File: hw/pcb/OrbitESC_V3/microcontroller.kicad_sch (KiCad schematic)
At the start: 63 parts, among them J1 USB_C_Receptacle_USB2.0, J11 CANH, J11 CANL, J11 GND, J11 RX, J11 TX, J8 Micro_SD_Card_Det2, SW1 Reset, SW2 DFU, U1 TLE9250X, U2 AT25SF128A-SHB-T, U3 STM32F446RETx, X1 ASE-24MHz

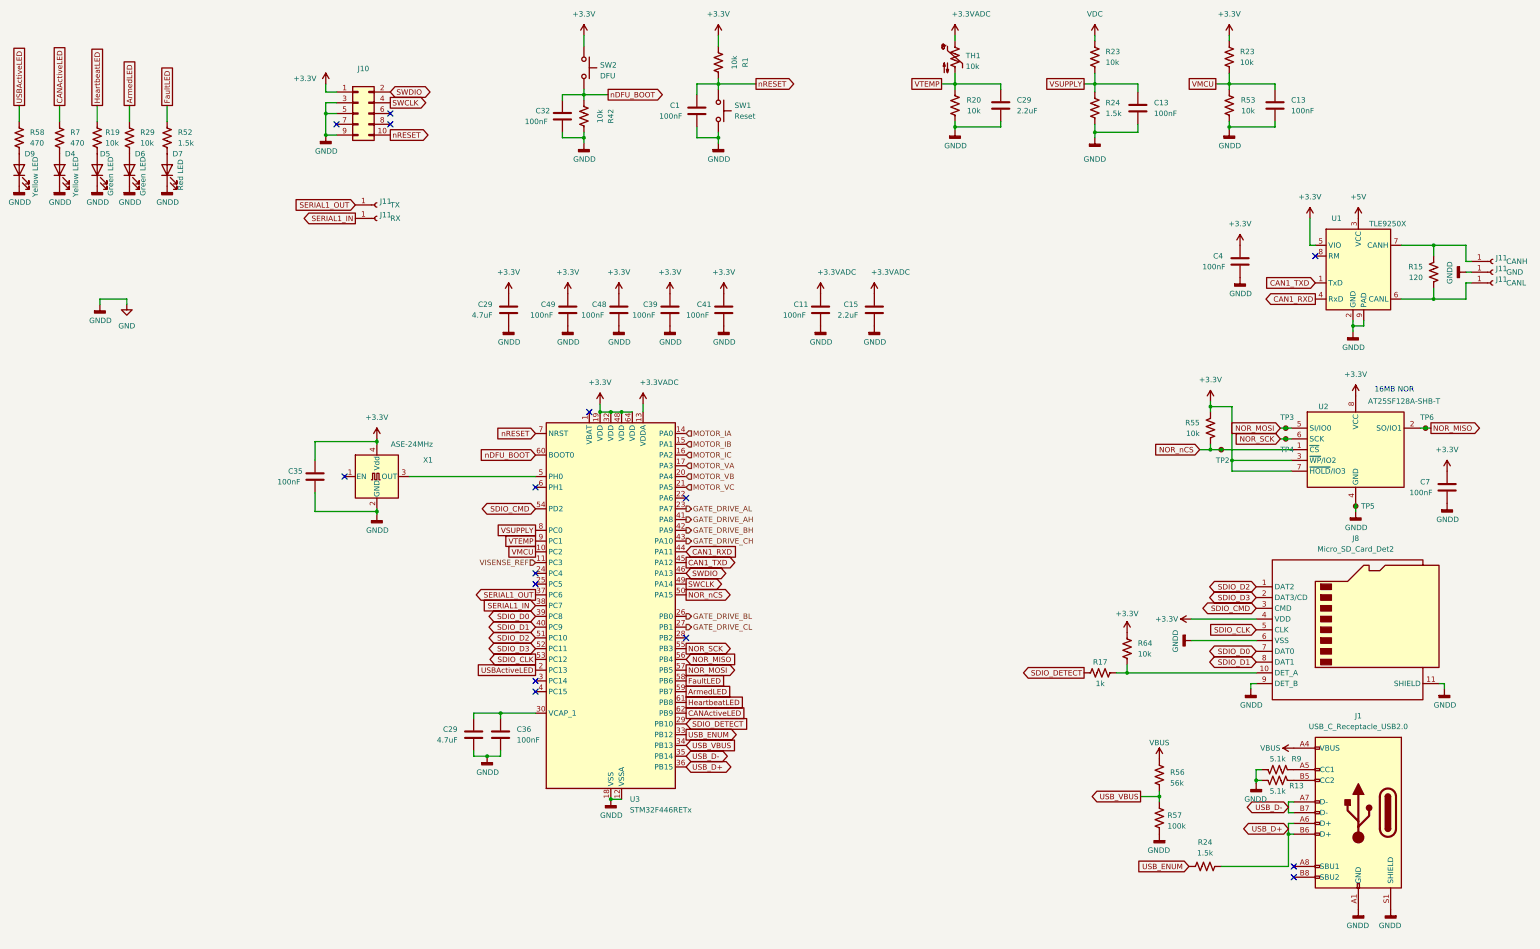
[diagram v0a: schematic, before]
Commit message: Finish initial draft of V3 pcb
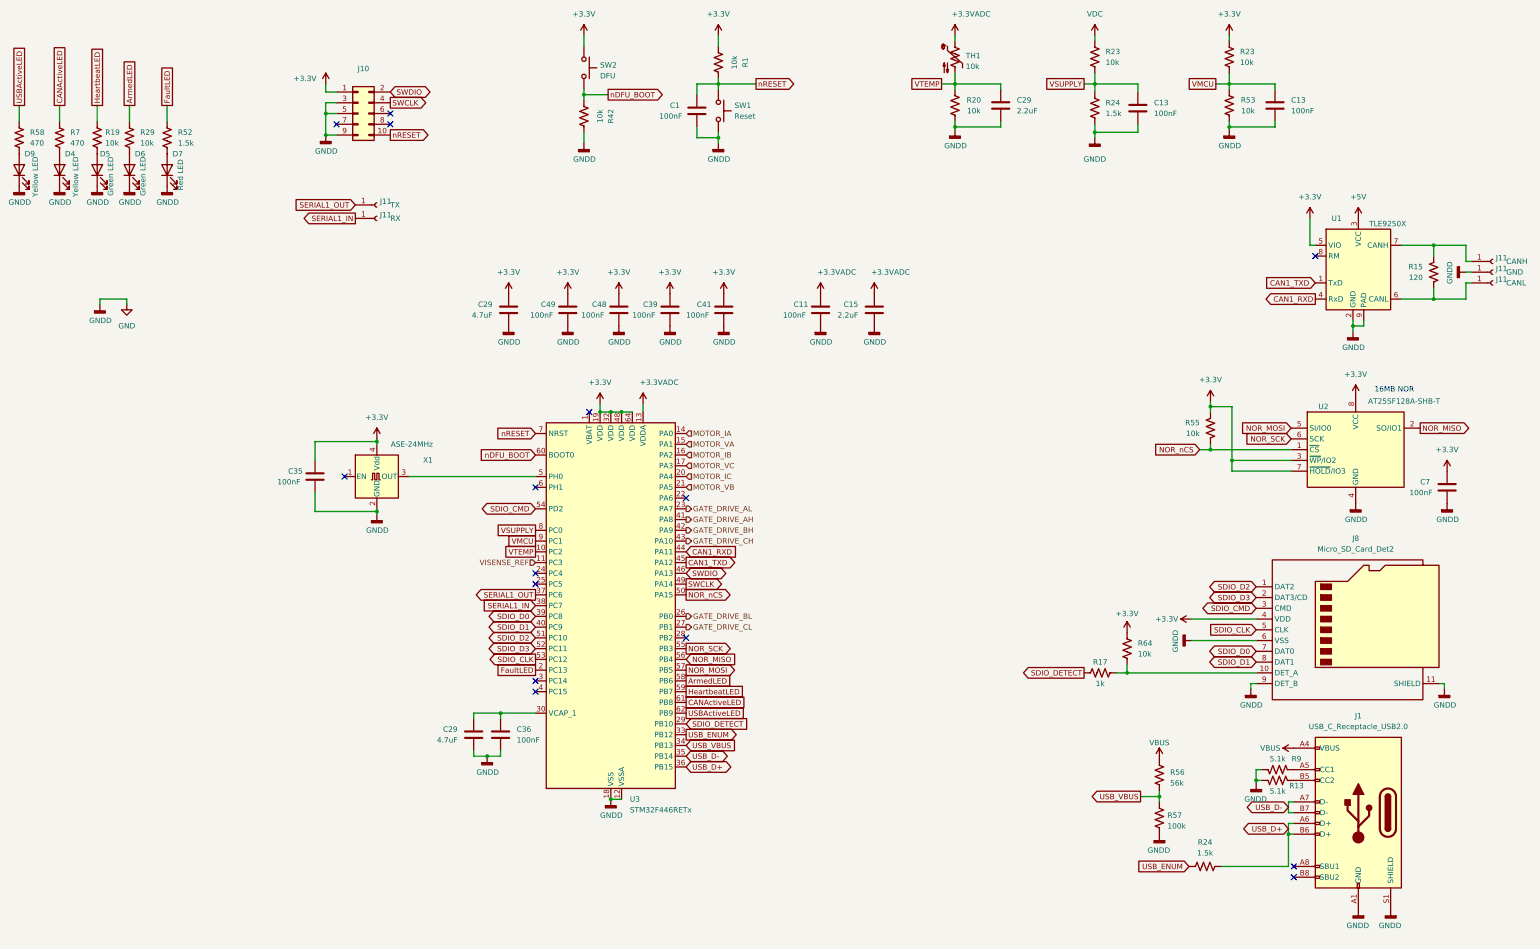
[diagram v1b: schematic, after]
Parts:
- removed C32, C4: 100nF, Capacitor_SMD:C_0402_1005Metric, symbol Device:C
- removed TP2: NOR_nCS, TestPoint:TestPoint_Pad_D1.0mm, symbol Connector:TestPoint_Small
- removed TP3: NOR_MOSI, TestPoint:TestPoint_Pad_D1.0mm, symbol Connector:TestPoint_Small
- removed TP4: NOR_SCK, TestPoint:TestPoint_Pad_D1.0mm, symbol Connector:TestPoint_Small
- removed TP5, TP6: NOR_MISO, TestPoint:TestPoint_Pad_D1.0mm, symbol Connector:TestPoint_Small
- R56, R57: footprint (none) -> Resistor_SMD:R_0402_1005Metric
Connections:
- net ArmedLED: now also U3.58 (PB6); no longer U3.59 (PB7)
- net CANActiveLED: now also U3.61 (PB8); no longer U3.62 (PB9)
- net FaultLED: now also U3.2 (PC13); no longer U3.58 (PB6)
- net HeartbeatLED: now also U3.59 (PB7); no longer U3.61 (PB8)
- net MOTOR_IB: now also U3.16 (PA2); no longer U3.15 (PA1)
- net MOTOR_IC: now also U3.20 (PA4); no longer U3.16 (PA2)
- net MOTOR_VA: now also U3.15 (PA1); no longer U3.17 (PA3)
- net MOTOR_VB: now also U3.21 (PA5); no longer U3.20 (PA4)
- net MOTOR_VC: now also U3.17 (PA3); no longer U3.21 (PA5)
- net USBActiveLED: now also U3.62 (PB9); no longer U3.2 (PC13)
- net VMCU: now also U3.9 (PC1); no longer U3.10 (PC2)
- net VTEMP: now also U3.10 (PC2); no longer U3.9 (PC1)

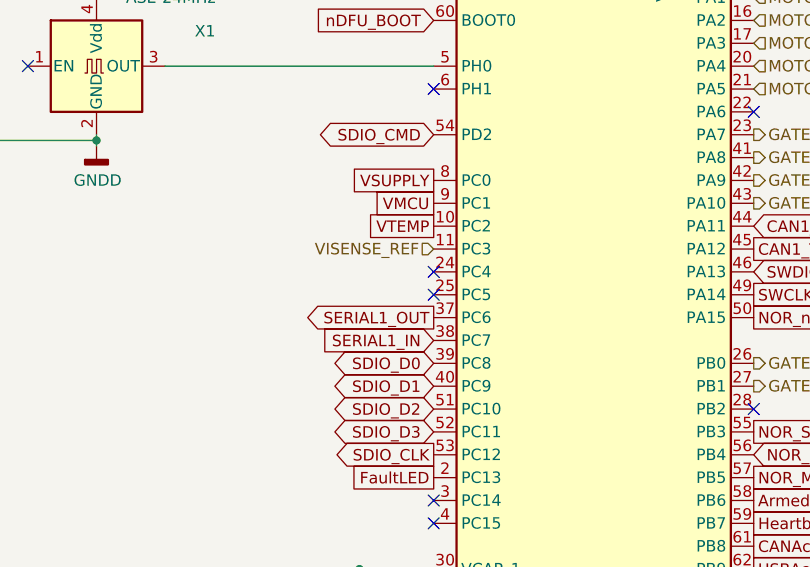
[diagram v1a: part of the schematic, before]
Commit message: Finalize PCB. Ordered it.
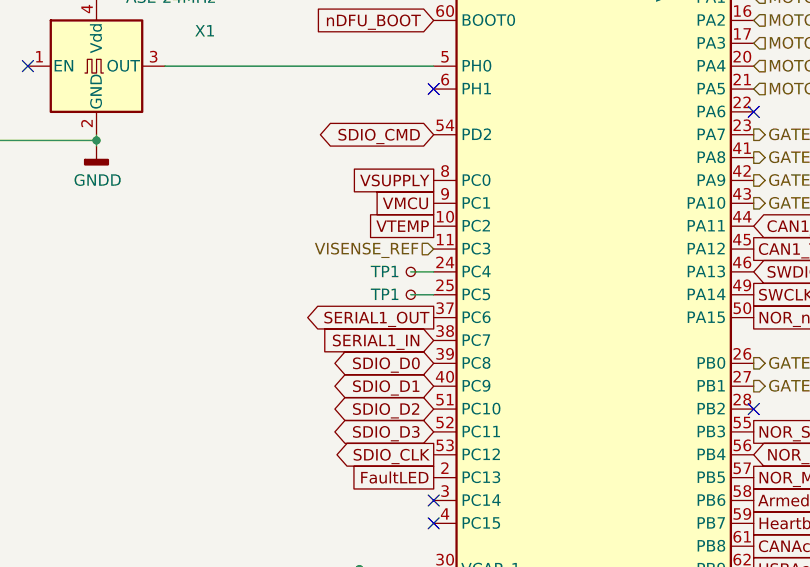
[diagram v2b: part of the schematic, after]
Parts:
- added TP1 (x2): CH, TestPoint:TestPoint_Pad_D1.0mm, symbol Connector:TestPoint_Small
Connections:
- net at U3.24 (PC4): now also TP1.1
- net at U3.25 (PC5): now also TP1.1
- no-connect marks 15 -> 13
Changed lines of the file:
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@@
   (no_connect (at 339.09 239.395))
   (no_connect (at 160.02 195.58))
-  (no_connect (at 160.02 167.64))
   (no_connect (at 172.72 129.54))
   (no_connect (at 114.935 144.78))
-  (no_connect (at 160.02 170.18))
   (wire (pts (xy 145.415 201.93) (xy 145.415 200.66))
     (stroke (width 0) (type default))
@@
     (stroke (width 0) (type default))
   )
+  (wire (pts (xy 157.48 170.18) (xy 160.02 170.18))
+    (stroke (width 0) (type default))
+  )
   (wire (pts (xy 122.555 135.89) (xy 122.555 136.525))
     (stroke (width 0) (type default))
@@
   )
   (wire (pts (xy 110.49 56.515) (xy 110.49 59.055))
+    (stroke (width 0) (type default))
+  )
+  (wire (pts (xy 157.48 167.64) (xy 160.02 167.64))
     (stroke (width 0) (type default))
   )
@@
     )
   )
+  (symbol (lib_id "Connector:TestPoint_Small") (at 157.48 170.18 0) (unit 1)
+    (in_bom yes) (on_board yes) (dnp no)
+    (property "Reference" "TP1" (at 153.035 170.18 0)
+      (effects (font (size 1.27 1.27)) (justify left))
+    )
+    (property "Value" "CH" (at 158.623 171.8822 0)
+      (effects (font (size 1.27 1.27)) (justify left) hide)
+    )
+    (property "Footprint" "TestPoint:TestPoint_Pad_D1.0mm" (at 162.56 170.18 0)
+      (effects (font (size 1.27 1.27)) hide)
+    )
+    (property "Datasheet" "~" (at 162.56 170.18 0)
+      (effects (font (size 1.27 1.27)) hide)
+    )
+    (property "DigiKey" "N/A" (at 157.48 170.18 0)
+      (effects (font (size 1.27 1.27)) hide)
+    )
+    (pin "1")
+    (instances
+      (project "OrbitESC"
+        (path "/a13534e1-2c37-4692-a99c-4eada4007967/968088fb-1c16-45c3-b31d-62fbdb9fdbdd"
+          (reference "TP1") (unit 1)
+        )
+        (path "/a13534e1-2c37-4692-a99c-4eada4007967/ed067bb8-caa7-448e-917b-cc2d33c8b4b7"
+          (reference "TP2") (unit 1)
+        )
+      )
+    )
+  )
   (symbol (lib_id "Device:C") (at 179.705 105.41 180) (unit 1)
     (in_bom yes) (on_board yes) (dnp no)
@@
         )
       )
+    )
+  )
+  (symbol (lib_id "Connector:TestPoint_Small") (at 157.48 167.64 0) (unit 1)
+    (in_bom yes) (on_board yes) (dnp no)
+    (property "Reference" "TP1" (at 153.035 167.64 0)
+      (effects (font (size 1.27 1.27)) (justify left))
+    )
+    (property "Value" "CH" (at 158.623 169.3422 0)
+      (effects (font (size 1.27 1.27)) (justify left) hide)
+    )
+    (property "Footprint" "TestPoint:TestPoint_Pad_D1.0mm" (at 162.56 167.64 0)
+      (effects (font (size 1.27 1.27)) hide)
+    )
+    (property "Datasheet" "~" (at 162.56 167.64 0)
+      (effects (font (size 1.27 1.27)) hide)
+    )
+    (property "DigiKey" "N/A" (at 157.48 167.64 0)
+      (effects (font (size 1.27 1.27)) hide)
+    )
+    (pin "1")
+    (instances
+      (project "OrbitESC"
+        (path "/a13534e1-2c37-4692-a99c-4eada4007967/968088fb-1c16-45c3-b31d-62fbdb9fdbdd"
+          (reference "TP1") (unit 1)
+        )
+        (path "/a13534e1-2c37-4692-a99c-4eada4007967/ed067bb8-caa7-448e-917b-cc2d33c8b4b7"
+          (reference "TP1") (unit 1)
+        )
+      )

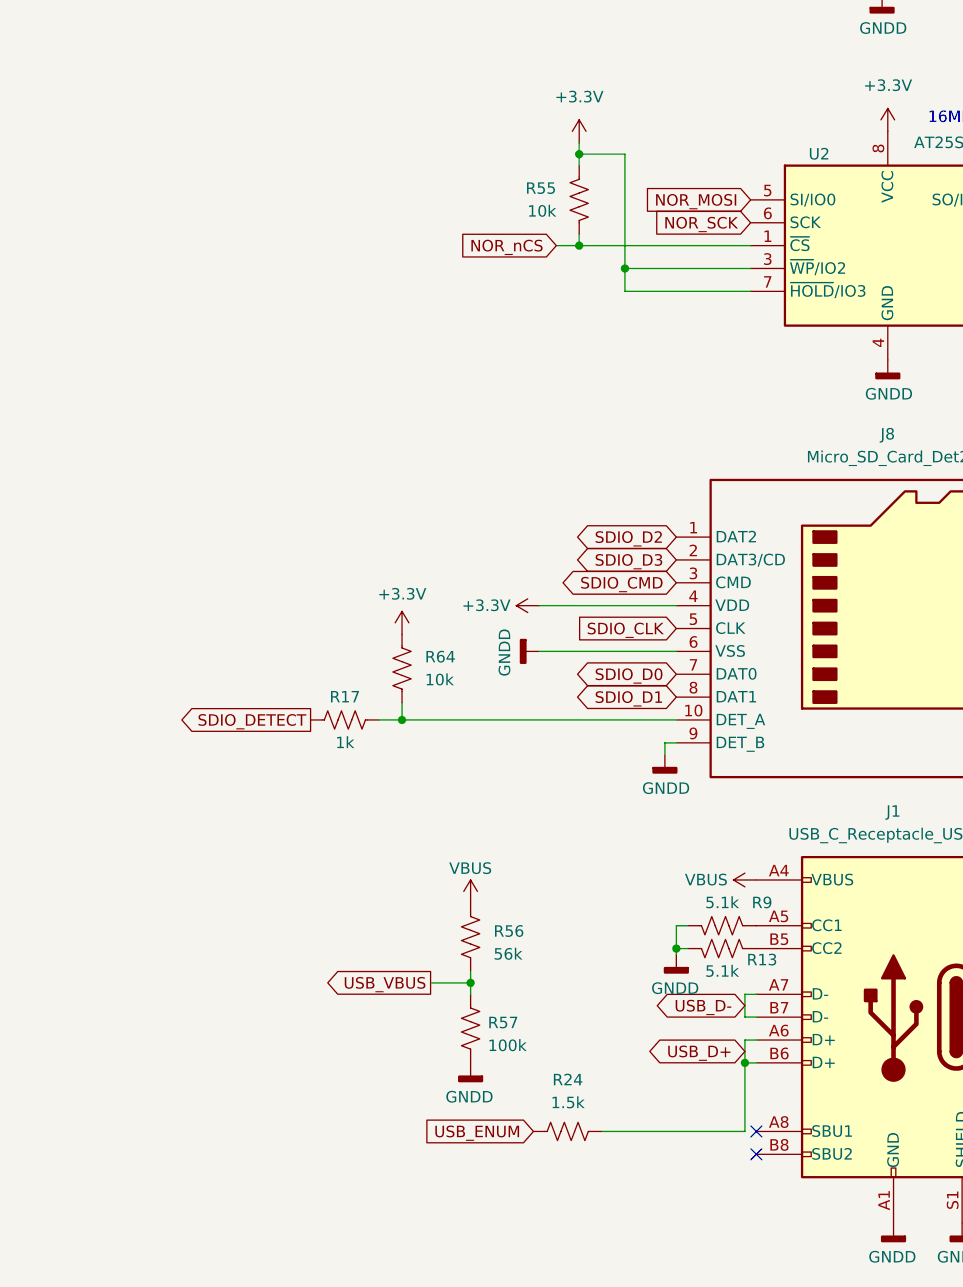
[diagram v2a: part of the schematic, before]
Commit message: Update schematic with a few discoveries from board bringup
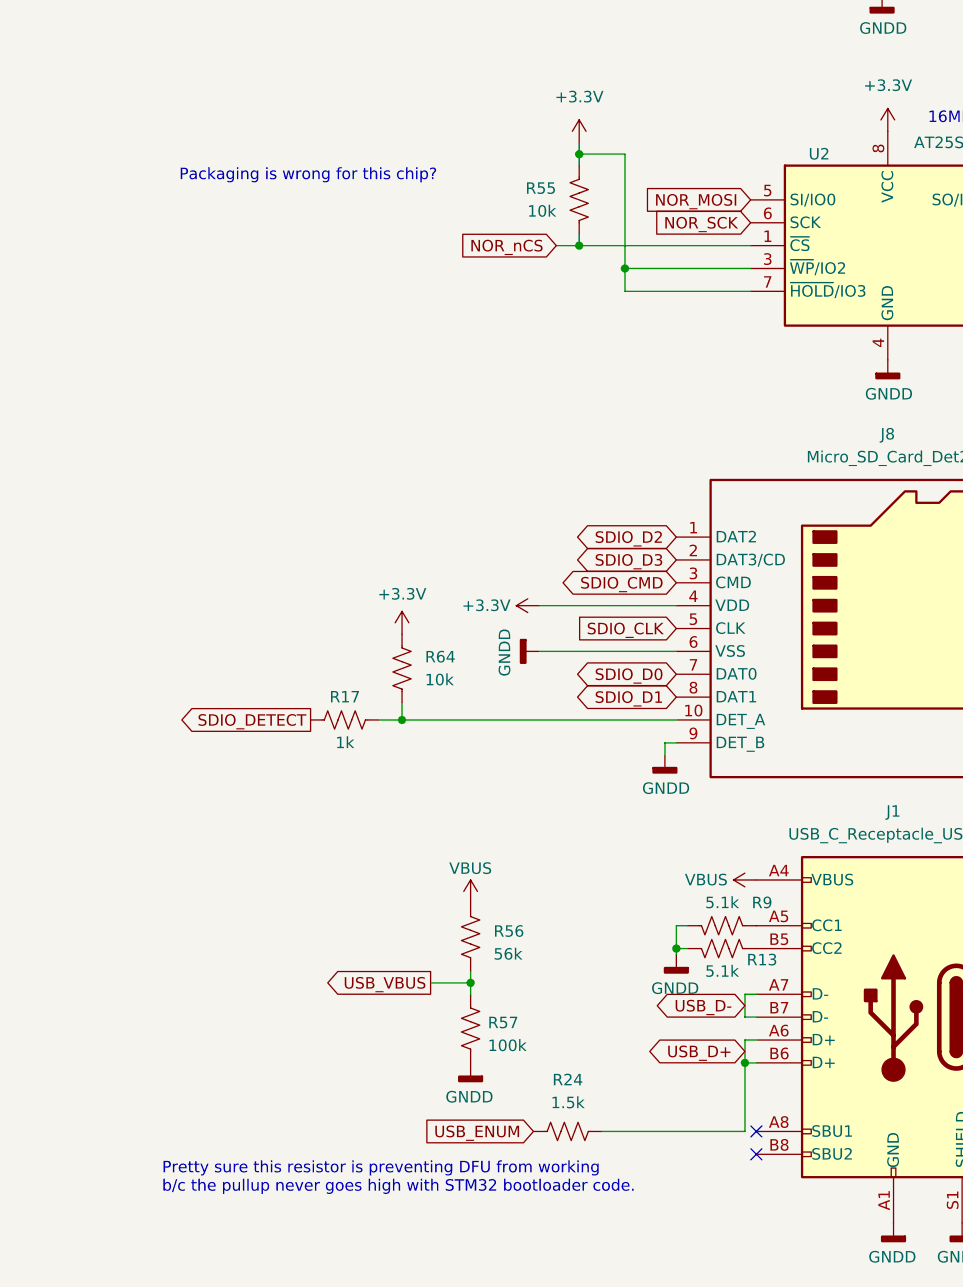
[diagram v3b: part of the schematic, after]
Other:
- note added: "Packaging is wrong for this chip?"
- note added: "Pretty sure this resistor is preventing DFU from working b/c the pullup never goes high with STM32 bootloader code."
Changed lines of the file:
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@@
     (stroke (width 0) (type default))
+  )
+  (text "Packaging is wrong for this chip?" (at 274.955 131.445 0)
+    (effects (font (size 1.27 1.27)) (justify left bottom))
+  )
+  (text "Pretty sure this resistor is preventing DFU from working\nb/c the pullup never goes high with STM32 bootloader code."
+    (at 273.05 243.84 0)
+    (effects (font (size 1.27 1.27)) (justify left bottom))
   )
   (text "16MB NOR" (at 358.14 125.095 0)

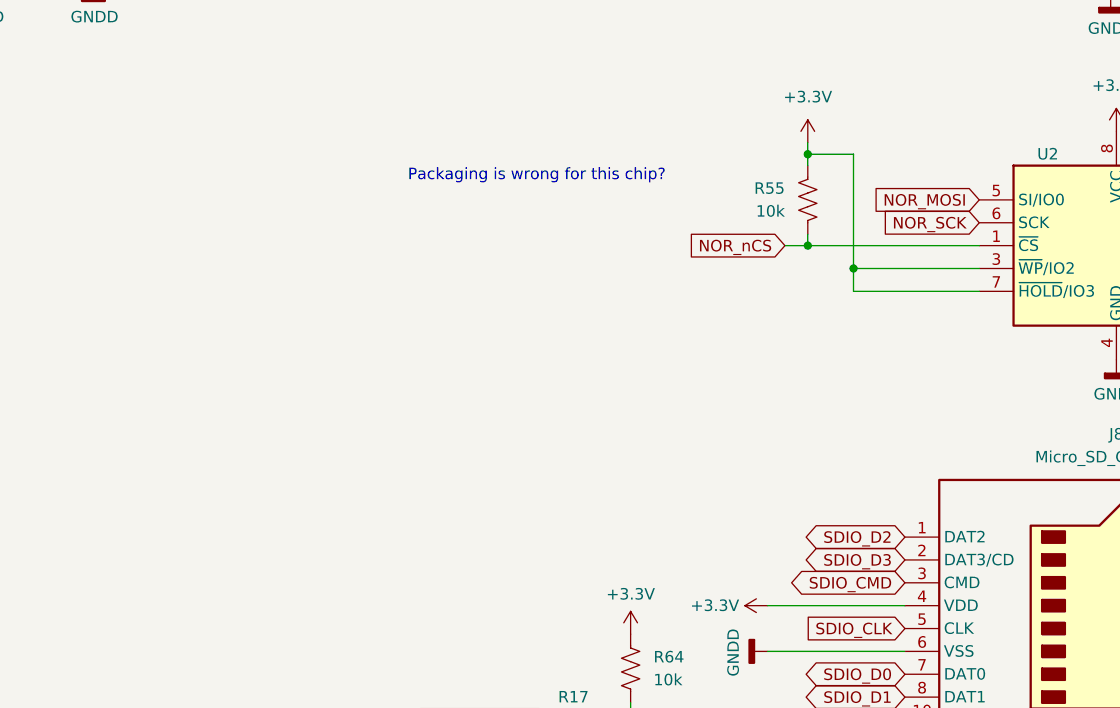
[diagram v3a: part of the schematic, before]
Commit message: First successful mounting of SD card
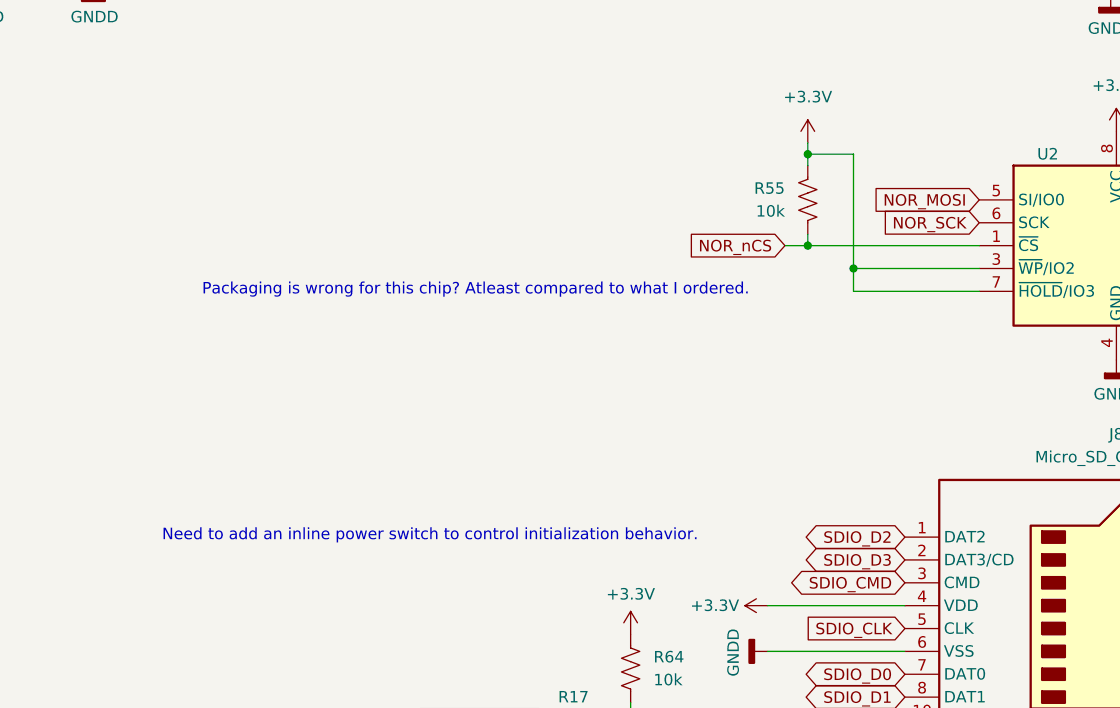
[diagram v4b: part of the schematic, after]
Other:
- note added: "Need to add an inline power switch to control initialization behavior."
- note added: "Packaging is wrong for this chip? Atleast compared to what I ordered."
- note removed: "Packaging is wrong for this chip?"
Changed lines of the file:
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@@
     (stroke (width 0) (type default))
   )
-  (text "Packaging is wrong for this chip?" (at 274.955 131.445 0)
+  (text "Need to add an inline power switch to control initialization behavior."
+    (at 247.65 171.45 0)
     (effects (font (size 1.27 1.27)) (justify left bottom))
   )
+  (text "Packaging is wrong for this chip? Atleast compared to what I ordered."
+    (at 252.095 144.145 0)
+    (effects (font (size 1.27 1.27)) (justify left bottom))
+  )
